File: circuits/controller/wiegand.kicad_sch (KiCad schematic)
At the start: 16 parts, among them Q10 Q_MMBT5551, Q11 Q_MMBT5551, Q12 Q_MMBT5551, Q13 Q_MMBT5551, Q14 Q_MMBT5551, Q15 Q_MMBT5551

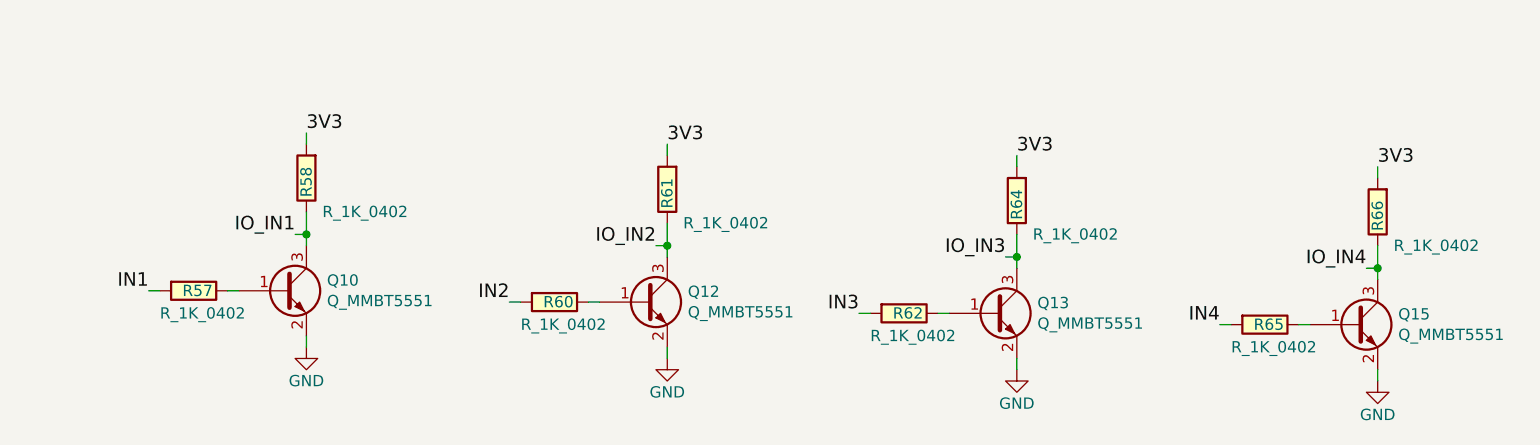
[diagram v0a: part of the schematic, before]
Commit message: fix(hardware): correct Wiegand input biasing
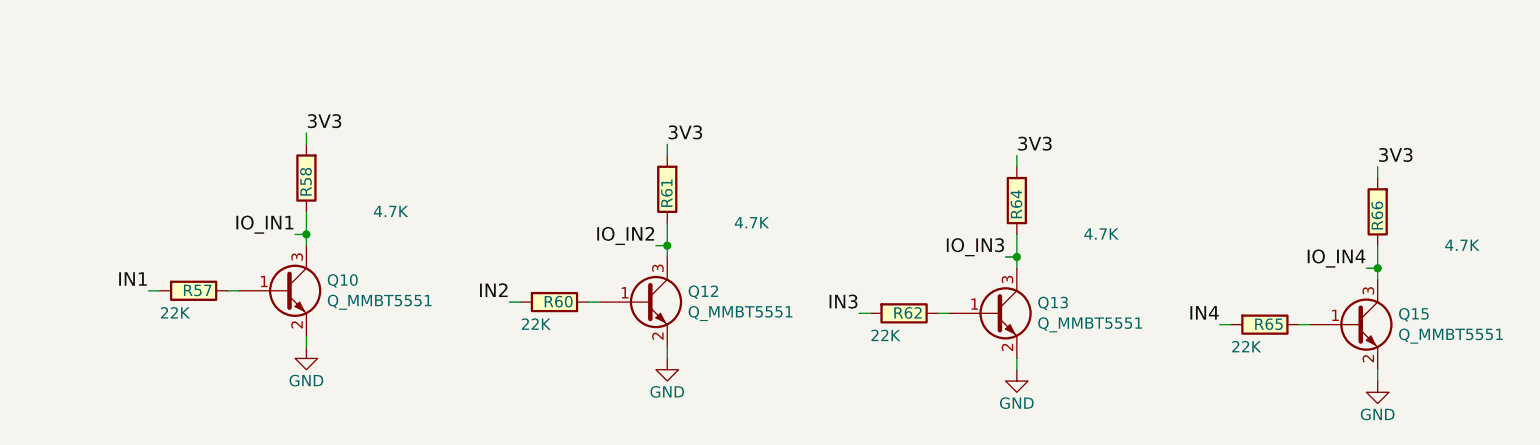
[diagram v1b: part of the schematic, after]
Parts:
- R57, R60, R62, R65: value R_1K_0402 -> 22K; LCSC C11702 -> C25768; Part Number 0402WGF1001TCE -> 0402WGF2202TCE
- R58, R61, R64, R66: value R_1K_0402 -> 4.7K; LCSC C11702 -> C25900; Part Number 0402WGF1001TCE -> 0402WGF4701TCE
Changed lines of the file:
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@@
       (effects (font (size 1.27 1.27)) (justify left))
     )
-    (property "Value" "R_1K_0402" (at 145.415 106.045 0)
+    (property "Value" "4.7K" (at 145.415 106.045 0)
       (effects (font (size 1.27 1.27)) (justify left))
     )
@@
       (effects (font (size 1.27 1.27)) hide)
     )
-    (property "Datasheet" "https://www.digikey.com/product-detail/en/panasonic-electronic-components/ERJ-3GEYJ102V/P1.0KGDKR-ND/577615" (at 131.953 102.235 90)
-      (effects (font (size 1.27 1.27)) hide)
-    )
-    (property "Part Number" "0402WGF1001TCE" (at 129.413 104.775 90)
-      (effects (font (size 1.524 1.524)) hide)
-    )
-    (property "LCSC" "C11702" (at 133.985 102.235 0)
+    (property "Datasheet" "https://www.lcsc.com/product-detail/C25900.html" (at 131.953 102.235 90)
+      (effects (font (size 1.27 1.27)) hide)
+    )
+    (property "Part Number" "0402WGF4701TCE" (at 129.413 104.775 90)
+      (effects (font (size 1.524 1.524)) hide)
+    )
+    (property "LCSC" "C25900" (at 133.985 102.235 0)
       (effects (font (size 1.27 1.27)) hide)
     )
@@
       (effects (font (size 1.27 1.27)) (justify left))
     )
-    (property "Value" "R_1K_0402" (at 104.775 104.775 0)
+    (property "Value" "4.7K" (at 104.775 104.775 0)
       (effects (font (size 1.27 1.27)) (justify left))
     )
@@
       (effects (font (size 1.27 1.27)) hide)
     )
-    (property "Datasheet" "https://www.digikey.com/product-detail/en/panasonic-electronic-components/ERJ-3GEYJ102V/P1.0KGDKR-ND/577615" (at 91.313 100.965 90)
-      (effects (font (size 1.27 1.27)) hide)
-    )
-    (property "Part Number" "0402WGF1001TCE" (at 88.773 103.505 90)
-      (effects (font (size 1.524 1.524)) hide)
-    )
-    (property "LCSC" "C11702" (at 93.345 100.965 0)
+    (property "Datasheet" "https://www.lcsc.com/product-detail/C25900.html" (at 91.313 100.965 90)
+      (effects (font (size 1.27 1.27)) hide)
+    )
+    (property "Part Number" "0402WGF4701TCE" (at 88.773 103.505 90)
+      (effects (font (size 1.524 1.524)) hide)
+    )
+    (property "LCSC" "C25900" (at 93.345 100.965 0)
       (effects (font (size 1.27 1.27)) hide)
     )
@@
       (effects (font (size 1.27 1.27)) (justify left))
     )
-    (property "Value" "R_1K_0402" (at 156.845 118.745 90)
+    (property "Value" "22K" (at 156.845 118.745 90)
       (effects (font (size 1.27 1.27)) (justify left))
     )
@@
       (effects (font (size 1.27 1.27)) hide)
     )
-    (property "Datasheet" "https://www.digikey.com/product-detail/en/panasonic-electronic-components/ERJ-3GEYJ102V/P1.0KGDKR-ND/577615" (at 160.655 118.237 90)
-      (effects (font (size 1.27 1.27)) hide)
-    )
-    (property "Part Number" "0402WGF1001TCE" (at 163.195 120.777 90)
-      (effects (font (size 1.524 1.524)) hide)
-    )
-    (property "LCSC" "C11702" (at 160.655 116.205 0)
+    (property "Datasheet" "https://www.lcsc.com/product-detail/Chip-Resistor-Surface-Mount_Uniroyal-Elec-0402WGF2202TCE_C25768.html" (at 160.655 118.237 90)
+      (effects (font (size 1.27 1.27)) hide)
+    )
+    (property "Part Number" "0402WGF2202TCE" (at 163.195 120.777 90)
+      (effects (font (size 1.524 1.524)) hide)
+    )
+    (property "LCSC" "C25768" (at 160.655 116.205 0)
       (effects (font (size 1.27 1.27)) hide)
     )
@@
       (effects (font (size 1.27 1.27)) (justify left))
     )
-    (property "Value" "R_1K_0402" (at 225.425 108.585 0)
+    (property "Value" "4.7K" (at 225.425 108.585 0)
       (effects (font (size 1.27 1.27)) (justify left))
     )
@@
       (effects (font (size 1.27 1.27)) hide)
     )
-    (property "Datasheet" "https://www.digikey.com/product-detail/en/panasonic-electronic-components/ERJ-3GEYJ102V/P1.0KGDKR-ND/577615" (at 211.963 104.775 90)
-      (effects (font (size 1.27 1.27)) hide)
-    )
-    (property "Part Number" "0402WGF1001TCE" (at 209.423 107.315 90)
-      (effects (font (size 1.524 1.524)) hide)
-    )
-    (property "LCSC" "C11702" (at 213.995 104.775 0)
+    (property "Datasheet" "https://www.lcsc.com/product-detail/C25900.html" (at 211.963 104.775 90)
+      (effects (font (size 1.27 1.27)) hide)
+    )
+    (property "Part Number" "0402WGF4701TCE" (at 209.423 107.315 90)
+      (effects (font (size 1.524 1.524)) hide)
+    )
+    (property "LCSC" "C25900" (at 213.995 104.775 0)
       (effects (font (size 1.27 1.27)) hide)
     )
@@
       (effects (font (size 1.27 1.27)) (justify left))
     )
-    (property "Value" "R_1K_0402" (at 184.785 107.315 0)
+    (property "Value" "4.7K" (at 184.785 107.315 0)
       (effects (font (size 1.27 1.27)) (justify left))
     )
@@
       (effects (font (size 1.27 1.27)) hide)
     )
-    (property "Datasheet" "https://www.digikey.com/product-detail/en/panasonic-electronic-components/ERJ-3GEYJ102V/P1.0KGDKR-ND/577615" (at 171.323 103.505 90)
-      (effects (font (size 1.27 1.27)) hide)
-    )
-    (property "Part Number" "0402WGF1001TCE" (at 168.783 106.045 90)
-      (effects (font (size 1.524 1.524)) hide)
-    )
-    (property "LCSC" "C11702" (at 173.355 103.505 0)
+    (property "Datasheet" "https://www.lcsc.com/product-detail/C25900.html" (at 171.323 103.505 90)
+      (effects (font (size 1.27 1.27)) hide)
+    )
+    (property "Part Number" "0402WGF4701TCE" (at 168.783 106.045 90)
+      (effects (font (size 1.524 1.524)) hide)
+    )
+    (property "LCSC" "C25900" (at 173.355 103.505 0)
       (effects (font (size 1.27 1.27)) hide)
     )
@@
       (effects (font (size 1.27 1.27)) (justify left))
     )
-    (property "Value" "R_1K_0402" (at 197.485 120.015 90)
+    (property "Value" "22K" (at 197.485 120.015 90)
       (effects (font (size 1.27 1.27)) (justify left))
     )
@@
       (effects (font (size 1.27 1.27)) hide)
     )
-    (property "Datasheet" "https://www.digikey.com/product-detail/en/panasonic-electronic-components/ERJ-3GEYJ102V/P1.0KGDKR-ND/577615" (at 201.295 119.507 90)
-      (effects (font (size 1.27 1.27)) hide)
-    )
-    (property "Part Number" "0402WGF1001TCE" (at 203.835 122.047 90)
-      (effects (font (size 1.524 1.524)) hide)
-    )
-    (property "LCSC" "C11702" (at 201.295 117.475 0)
+    (property "Datasheet" "https://www.lcsc.com/product-detail/Chip-Resistor-Surface-Mount_Uniroyal-Elec-0402WGF2202TCE_C25768.html" (at 201.295 119.507 90)
+      (effects (font (size 1.27 1.27)) hide)
+    )
+    (property "Part Number" "0402WGF2202TCE" (at 203.835 122.047 90)
+      (effects (font (size 1.524 1.524)) hide)
+    )
+    (property "LCSC" "C25768" (at 201.295 117.475 0)
       (effects (font (size 1.27 1.27)) hide)
     )
@@
       (effects (font (size 1.27 1.27)) (justify left))
     )
-    (property "Value" "R_1K_0402" (at 117.475 117.475 90)
+    (property "Value" "22K" (at 117.475 117.475 90)
       (effects (font (size 1.27 1.27)) (justify left))
     )
@@
       (effects (font (size 1.27 1.27)) hide)
     )
-    (property "Datasheet" "https://www.digikey.com/product-detail/en/panasonic-electronic-components/ERJ-3GEYJ102V/P1.0KGDKR-ND/577615" (at 121.285 116.967 90)
-      (effects (font (size 1.27 1.27)) hide)
-    )
-    (property "Part Number" "0402WGF1001TCE" (at 123.825 119.507 90)
-      (effects (font (size 1.524 1.524)) hide)
-    )
-    (property "LCSC" "C11702" (at 121.285 114.935 0)
+    (property "Datasheet" "https://www.lcsc.com/product-detail/Chip-Resistor-Surface-Mount_Uniroyal-Elec-0402WGF2202TCE_C25768.html" (at 121.285 116.967 90)
+      (effects (font (size 1.27 1.27)) hide)
+    )
+    (property "Part Number" "0402WGF2202TCE" (at 123.825 119.507 90)
+      (effects (font (size 1.524 1.524)) hide)
+    )
+    (property "LCSC" "C25768" (at 121.285 114.935 0)
       (effects (font (size 1.27 1.27)) hide)
     )
@@
       (effects (font (size 1.27 1.27)) (justify left))
     )
-    (property "Value" "R_1K_0402" (at 76.835 116.205 90)
+    (property "Value" "22K" (at 76.835 116.205 90)
       (effects (font (size 1.27 1.27)) (justify left))
     )
@@
       (effects (font (size 1.27 1.27)) hide)
     )
-    (property "Datasheet" "https://www.digikey.com/product-detail/en/panasonic-electronic-components/ERJ-3GEYJ102V/P1.0KGDKR-ND/577615" (at 80.645 115.697 90)
-      (effects (font (size 1.27 1.27)) hide)
-    )
-    (property "Part Number" "0402WGF1001TCE" (at 83.185 118.237 90)
-      (effects (font (size 1.524 1.524)) hide)
-    )
-    (property "LCSC" "C11702" (at 80.645 113.665 0)
-      (effects (font (size 1.27 1.27)) hide)
-    )
+    (property "Datasheet" "https://www.lcsc.com/product-detail/Chip-Resistor-Surface-Mount_Uniroyal-Elec-0402WGF2202TCE_C25768.html" (at 80.645 115.697 90)
+      (effects (font (size 1.27 1.27)) hide)
+    )
+    (property "Part Number" "0402WGF2202TCE" (at 83.185 118.237 90)
+      (effects (font (size 1.524 1.524)) hide)
+    )
+    (property "LCSC" "C25768" (at 80.645 113.665 0)
+      (effects (font (size 1.27 1.27)) hide)
+    )
